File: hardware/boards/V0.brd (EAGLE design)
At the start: 134 parts, among them IC2 TPS6300, J1 SJ-43515TS-SMT, J2 HIROSE_DM3BT-DSF-PEJSHIROSE_D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, J3 MOLEX_105450-0101MOLEX_105450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, Q2 ON_SEMI_MMBT5551LT1GON_SEMI_M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, U1 VS1053-L, U2 MICROCHIP_MCP73831T-2ATI-OTMI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, X3 FH12-45S-0.5SH

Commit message: schematic: done!?
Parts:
- R31: value 1k -> 2k
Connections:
- removed net BLUE_LED_CATH: D1.1
- removed net IO18: R8.1, U$1.35
- removed net N$42: U1.30
- removed net N$43: U1.29
- removed net N$44: U1.28
- removed net N$45: U1.23
- removed net N$46: U1.13
- removed net N$47: U1.8
- removed net VDD_SDIO: U$1.26
- new net DREQ: U$1.15, U1.8
- new net SPI_MISO: U$1.38, U1.30, X3.29
- new net VIB_MOTOR: R8.1, U$1.29
- new net VS_CMD_CS: U$1.16, U1.23
- new net VS_DATA_CS: U$1.34, U1.13
- net ATQ_CHANGE: now also U$1.14
- net BUTTON_ADC: now also U$1.10
- net BUTTON_DIN: now also U$1.8
- net CP_VDD: no longer C24.+, C25.+, R31.2
- net DISPLAY_CS: now also U$1.12
- net DISPLAY_RST: now also U$1.13
- net GND: now also J2.12, J2.13, J2.14, X3.3; no longer X3.31, X3.33
- net GREEN_LED_CATH: now also U$1.28
- net I2C_SCL: now also U$1.39
- net I2C_SDA: now also U$1.42
- net IO0: now also D1.1
- net IO12: now also U$1.18
- net IO13: now also U$1.20
- net IO14: now also R7.2, U$1.17; no longer R6.2
- net IO15: now also R6.2, U$1.21; no longer R7.2
- net IO2: now also U$1.22
- net IO4: now also U$1.24
- net SPI_CLK: now also U$1.35, U1.28
- net SPI_MOSI: now also U$1.36, U1.29
- net V3P3: now also C24.+, C25.+, R31.2, X3.31, X3.33
- net VBAT_ADC_IN: now also U$1.7

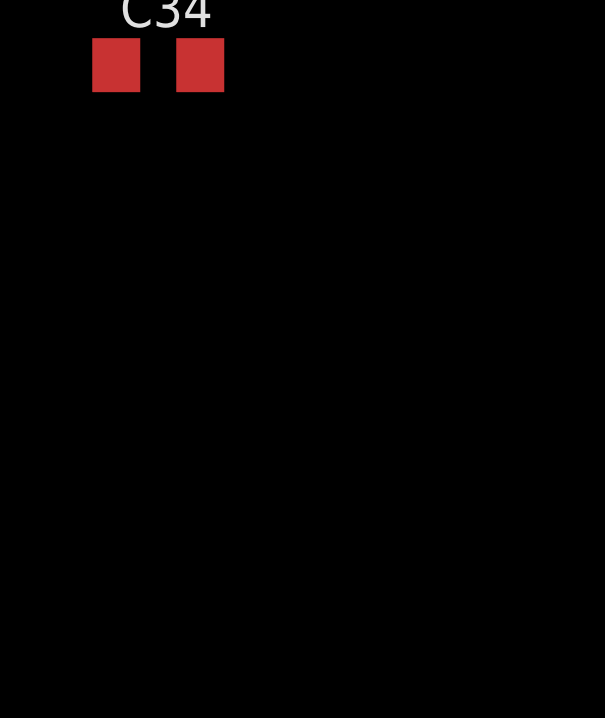
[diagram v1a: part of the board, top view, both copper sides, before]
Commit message: minor fixes: this is an adjustable 1.8V regulator..
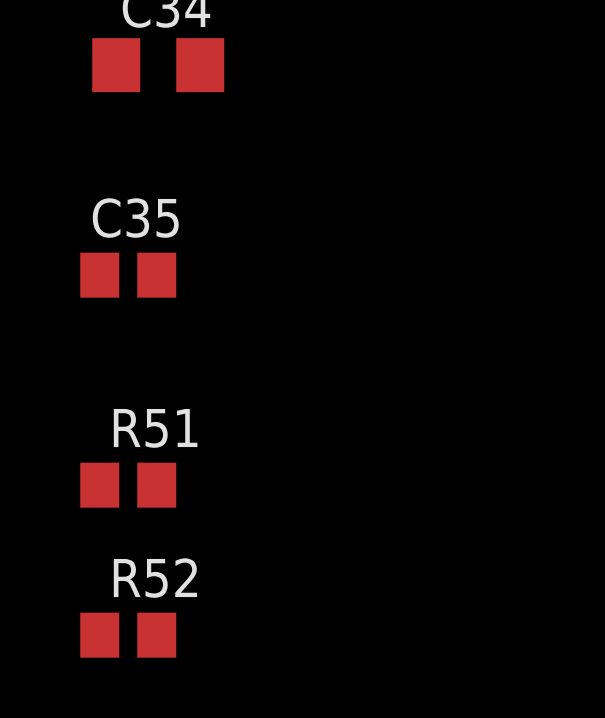
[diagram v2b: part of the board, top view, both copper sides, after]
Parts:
- added C35: 33pF, rcl:C0805
- added R51: 180k, rcl:R0805
- added R52: 360k, rcl:R0805
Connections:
- new net N$42: C35.2, R51.2, R52.1, TPS6224.5
- net GND: now also R51.1
- net V1P8: now also C35.1, R52.2; no longer TPS6224.5
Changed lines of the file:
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@@
 <attribute name="VALUE" x="-42.27" y="-778.54" size="1.27" layer="27"/>
+</element>
+<element name="C35" library="rcl" library_urn="urn:adsk.eagle:library:334" package="C0805" package3d_urn="urn:adsk.eagle:package:23617/2" value="33pF" x="-42" y="-783" smashed="yes">
+<attribute name="NAME" x="-43.27" y="-781.73" size="1.27" layer="25"/>
+<attribute name="SPICEPREFIX" value="C" x="-42" y="-783" size="1.778" layer="27" display="off"/>
+<attribute name="VALUE" x="-43.27" y="-785.54" size="1.27" layer="27"/>
+</element>
+<element name="R51" library="rcl" library_urn="urn:adsk.eagle:library:334" package="R0805" package3d_urn="urn:adsk.eagle:package:23553/2" value="180k" x="-42" y="-790" smashed="yes">
+<attribute name="NAME" x="-42.635" y="-788.73" size="1.27" layer="25"/>
+<attribute name="SPICEPREFIX" value="R" x="-42" y="-790" size="1.778" layer="27" display="off"/>
+<attribute name="VALUE" x="-42.635" y="-792.54" size="1.27" layer="27"/>
+</element>
+<element name="R52" library="rcl" library_urn="urn:adsk.eagle:library:334" package="R0805" package3d_urn="urn:adsk.eagle:package:23553/2" value="360k" x="-42" y="-795" smashed="yes">
+<attribute name="NAME" x="-42.635" y="-793.73" size="1.27" layer="25"/>
+<attribute name="SPICEPREFIX" value="R" x="-42" y="-795" size="1.778" layer="27" display="off"/>
+<attribute name="VALUE" x="-42.635" y="-797.54" size="1.27" layer="27"/>
 </element>
 </elements>
@@
 <contactref element="X3" pad="28"/>
 <contactref element="X3" pad="3"/>
+<contactref element="R51" pad="1"/>
 <wire x1="-21.275" y1="-222.175" x2="-28.675" y2="-222.175" width="0" layer="19" extent="1-1"/>
 <wire x1="-17.275" y1="-226.375" x2="-21.275" y2="-222.175" width="0" layer="19" extent="1-1"/>
@@
 <wire x1="-39.6" y1="-764" x2="-39.6" y2="-759" width="0" layer="19" extent="1-1"/>
 <wire x1="-39.6" y1="-776" x2="-39.6" y2="-764" width="0" layer="19" extent="1-1"/>
+<wire x1="-42.95" y1="-790" x2="-39.6" y2="-776" width="0" layer="19" extent="1-1"/>
 </signal>
 <signal name="N$22">
@@
 </signal>
 <signal name="V1P8">
-<contactref element="TPS6224" pad="5"/>
 <contactref element="U$5" pad="P$2"/>
 <contactref element="C18" pad="1"/>
@@
 <contactref element="TP2" pad="TP"/>
 <contactref element="C5" pad="1"/>
+<contactref element="C35" pad="1"/>
+<contactref element="R52" pad="2"/>
 <wire x1="-37.475" y1="-632" x2="-43" y2="-686" width="0" layer="19" extent="1-1"/>
+<wire x1="-42.95" y1="-783" x2="-43" y2="-686" width="0" layer="19" extent="1-1"/>
+<wire x1="-41.05" y1="-795" x2="-42.95" y2="-783" width="0" layer="19" extent="1-1"/>
 <wire x1="-20.7" y1="-336" x2="-37.475" y2="-632" width="0" layer="19" extent="1-1"/>
 <wire x1="-15.7" y1="-336" x2="-20.7" y2="-336" width="0" layer="19" extent="1-1"/>
@@
 <wire x1="-27.1" y1="-155.8" x2="-27.25" y2="-311.75" width="0" layer="19" extent="1-1"/>
 <wire x1="-30.4" y1="-143" x2="-27.1" y2="-155.8" width="0" layer="19" extent="1-1"/>
-<wire x1="-22.65" y1="-141.15" x2="-30.4" y2="-143" width="0" layer="19" extent="1-1"/>
 </signal>
 <signal name="N$3">
@@
 <wire x1="-14.725" y1="-7.75" x2="-23.95" y2="-81" width="0" layer="19" extent="1-1"/>
 </signal>
+<signal name="N$42">
+<contactref element="TPS6224" pad="5"/>
+<contactref element="R51" pad="2"/>
+<contactref element="C35" pad="2"/>
+<contactref element="R52" pad="1"/>
+<wire x1="-41.05" y1="-783" x2="-22.65" y2="-141.15" width="0" layer="19" extent="1-1"/>
+<wire x1="-41.05" y1="-790" x2="-41.05" y2="-783" width="0" layer="19" extent="1-1"/>
+<wire x1="-42.95" y1="-795" x2="-41.05" y2="-790" width="0" layer="19" extent="1-1"/>
+</signal>
 </signals>

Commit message: Power on/off changes + misc fixes
Corrected the power on/off circuit (connected the top of the switch to the right net) and bumped up the resistor value so that it'll take ~6 seconds of the power button being held down to power off.
The circuit should now match Figure 5 from [this](http://www.mosaic-industries.com/embedded-systems/microcontroller-projects/electronic-circuits/push-button-switch-turn-on/latching-toggle-power-switch).

This fixes #1.

Additionally, libraries used in the V0 files should match the rearranged folders.
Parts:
- R11: value 5M -> 10M
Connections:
- removed net CENTER_SW_PWR_BTM: CENTER_SW_PWR.4, CENTER_SW_PWR.4-2
- removed net N$12: C6.1, R10.1
- net CENTER_SW_PWR_TOP: now also C6.1, R10.1
- net GND: now also CENTER_SW_PWR.4, CENTER_SW_PWR.4-2
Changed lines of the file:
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@@
 <attribute name="VALUE" x="-22.775" y="-270.925" size="1.27" layer="27" rot="R90"/>
 </element>
-<element name="R11" library="rcl" library_urn="urn:adsk.eagle:library:334" package="R0805" package3d_urn="urn:adsk.eagle:package:23553/2" value="5M" x="-21" y="-275" smashed="yes">
+<element name="R11" library="rcl" library_urn="urn:adsk.eagle:library:334" package="R0805" package3d_urn="urn:adsk.eagle:package:23553/2" value="10M" x="-21" y="-275" smashed="yes">
 <attribute name="NAME" x="-22.397" y="-273.857" size="1.27" layer="25"/>
 <attribute name="SPICEPREFIX" value="R" x="-21" y="-275" size="1.778" layer="27" display="off"/>
@@
 <contactref element="X3" pad="3"/>
 <contactref element="R51" pad="1"/>
+<contactref element="CENTER_SW_PWR" pad="4"/>
+<contactref element="CENTER_SW_PWR" pad="4-2"/>
 <wire x1="-21.275" y1="-222.175" x2="-28.675" y2="-222.175" width="0" layer="19" extent="1-1"/>
 <wire x1="-17.275" y1="-226.375" x2="-21.275" y2="-222.175" width="0" layer="19" extent="1-1"/>
@@
 <wire x1="-35.05" y1="-548" x2="-35.05" y2="-541" width="0" layer="19" extent="1-1"/>
 <wire x1="-35.05" y1="-555" x2="-35.05" y2="-548" width="0" layer="19" extent="1-1"/>
-<wire x1="-42.525" y1="-632" x2="-35.05" y2="-555" width="0" layer="19" extent="1-1"/>
+<wire x1="-38.525" y1="-568.75" x2="-35.05" y2="-555" width="0" layer="19" extent="1-1"/>
+<wire x1="-38.875" y1="-568.75" x2="-38.525" y2="-568.75" width="0" layer="19" extent="1-1"/>
+<wire x1="-42.525" y1="-632" x2="-38.875" y2="-568.75" width="0" layer="19" extent="1-1"/>
 <wire x1="-42.525" y1="-638" x2="-42.525" y2="-632" width="0" layer="19" extent="1-1"/>
 <wire x1="-41.05" y1="-652" x2="-42.525" y2="-638" width="0" layer="19" extent="1-1"/>
@@
 <wire x1="-17.6" y1="-255" x2="-28.95" y2="-270.925" width="0" layer="19" extent="1-1"/>
 </signal>
-<signal name="N$12">
-<contactref element="R10" pad="1"/>
-<contactref element="C6" pad="1"/>
-<wire x1="-20.4" y1="-255" x2="-29.95" y2="-282" width="0" layer="19" extent="1-1"/>
-</signal>
 <signal name="N$14">
 <contactref element="C7" pad="2"/>
@@
 <contactref element="CENTER_SW_PWR" pad="2"/>
 <contactref element="R11" pad="1"/>
+<contactref element="R10" pad="1"/>
+<contactref element="C6" pad="1"/>
 <wire x1="-38.875" y1="-565.25" x2="-38.525" y2="-565.25" width="0" layer="19" extent="1-1"/>
-<wire x1="-21.95" y1="-275" x2="-38.525" y2="-565.25" width="0" layer="19" extent="1-1"/>
-</signal>
-<signal name="CENTER_SW_PWR_BTM">
-<contactref element="CENTER_SW_PWR" pad="4-2"/>
-<contactref element="CENTER_SW_PWR" pad="4"/>
-<wire x1="-38.875" y1="-568.75" x2="-38.525" y2="-568.75" width="0" layer="19" extent="1-1"/>
+<wire x1="-29.95" y1="-282" x2="-38.525" y2="-565.25" width="0" layer="19" extent="1-1"/>
+<wire x1="-21.95" y1="-275" x2="-29.95" y2="-282" width="0" layer="19" extent="1-1"/>
+<wire x1="-20.4" y1="-255" x2="-21.95" y2="-275" width="0" layer="19" extent="1-1"/>
 </signal>
 <signal name="N$18">

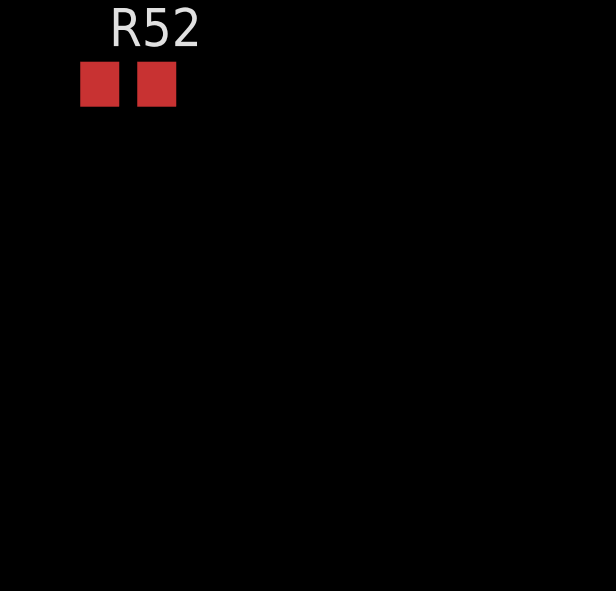
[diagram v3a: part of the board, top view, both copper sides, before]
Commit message: Add UVLO protection (using an APX809S-31SA)
Closes #4
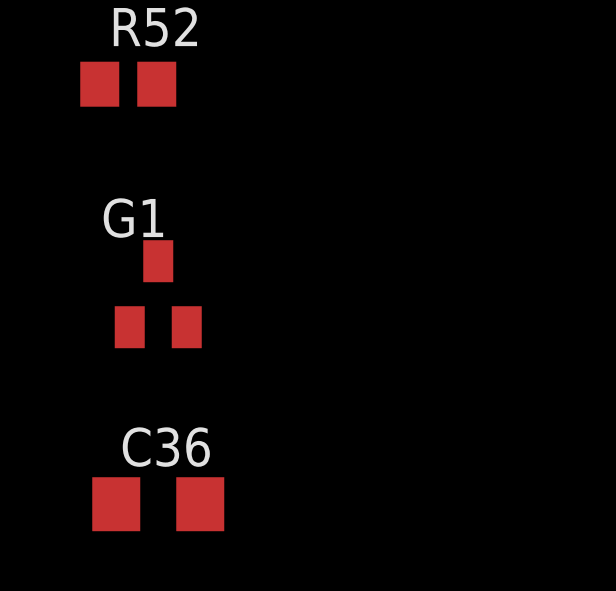
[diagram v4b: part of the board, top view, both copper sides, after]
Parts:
- added C36: 100nF, rcl:C1206
- added G1: APX809S-31SA, APX80xx:SOT23
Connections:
- new net N$12: U$2.3, U$2.5, U$2.7
- new net N$33: U$2.10, U$2.11, U$2.9
- new net N$43: G1.2, U$2.8
- net GND: now also C36.2, G1.1
- net SYS_ENABLE: now also U$2.12; no longer U$2.3, U$2.5
- net VBAT: now also C36.1, G1.3
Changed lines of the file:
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@@
 <attribute name="VALUE" x="-42.635" y="-797.54" size="1.27" layer="27"/>
+</element>
+<element name="G1" library="APX80xx" package="SOT23" package3d_urn="urn:adsk.eagle:package:28738/2" value="APX809S-31SA" x="-41" y="-802" smashed="yes">
+<attribute name="NAME" x="-42.905" y="-800.095" size="1.27" layer="25"/>
+<attribute name="VALUE" x="-42.905" y="-805.175" size="1.27" layer="27"/>
+</element>
+<element name="C36" library="rcl" library_urn="urn:adsk.eagle:library:334" package="C1206" package3d_urn="urn:adsk.eagle:package:23618/2" value="100nF" x="-41" y="-809" smashed="yes">
+<attribute name="NAME" x="-42.27" y="-807.73" size="1.27" layer="25"/>
+<attribute name="SPICEPREFIX" value="C" x="-41" y="-809" size="1.778" layer="27" display="off"/>
+<attribute name="VALUE" x="-42.27" y="-811.54" size="1.27" layer="27"/>
 </element>
 </elements>
@@
 <contactref element="CENTER_SW_PWR" pad="4"/>
 <contactref element="CENTER_SW_PWR" pad="4-2"/>
+<contactref element="G1" pad="1"/>
+<contactref element="C36" pad="2"/>
 <wire x1="-21.275" y1="-222.175" x2="-28.675" y2="-222.175" width="0" layer="19" extent="1-1"/>
 <wire x1="-17.275" y1="-226.375" x2="-21.275" y2="-222.175" width="0" layer="19" extent="1-1"/>
@@
 <wire x1="-39.6" y1="-776" x2="-39.6" y2="-764" width="0" layer="19" extent="1-1"/>
 <wire x1="-42.95" y1="-790" x2="-39.6" y2="-776" width="0" layer="19" extent="1-1"/>
+<wire x1="-41.95" y1="-803.1" x2="-42.95" y2="-790" width="0" layer="19" extent="1-1"/>
+<wire x1="-39.6" y1="-809" x2="-41.95" y2="-803.1" width="0" layer="19" extent="1-1"/>
 </signal>
 <signal name="N$22">
@@
 <contactref element="R10" pad="2"/>
 <contactref element="R9" pad="2"/>
+<contactref element="G1" pad="3"/>
+<contactref element="C36" pad="1"/>
 <wire x1="-18.05" y1="-156" x2="-27.5" y2="-162.95" width="0" layer="19" extent="1-1"/>
 <wire x1="-24.85" y1="-150" x2="-18.05" y2="-156" width="0" layer="19" extent="1-1"/>
@@
 <wire x1="-35.2" y1="-536.95" x2="-35.05" y2="-529" width="0" layer="19" extent="1-1"/>
 <wire x1="-36.95" y1="-541" x2="-35.2" y2="-536.95" width="0" layer="19" extent="1-1"/>
+<wire x1="-41" y1="-800.9" x2="-36.95" y2="-541" width="0" layer="19" extent="1-1"/>
+<wire x1="-42.4" y1="-809" x2="-41" y2="-800.9" width="0" layer="19" extent="1-1"/>
 </signal>
 <signal name="V3P3">
@@
 <signal name="SYS_ENABLE">
 <contactref element="IC2" pad="6"/>
-<contactref element="U$2" pad="3"/>
-<contactref element="U$2" pad="5"/>
-<wire x1="-26.35" y1="-270.925" x2="-18" y2="-128.525" width="0" layer="19" extent="1-1"/>
-<wire x1="-27.65" y1="-270.925" x2="-26.35" y2="-270.925" width="0" layer="19" extent="1-1"/>
+<contactref element="U$2" pad="12"/>
+<wire x1="-27.65" y1="-265.075" x2="-18" y2="-128.525" width="0" layer="19" extent="1-1"/>
 </signal>
 <signal name="CENTER_SW_PWR_TOP">
@@
 <wire x1="-42.95" y1="-795" x2="-41.05" y2="-790" width="0" layer="19" extent="1-1"/>
 </signal>
+<signal name="N$12">
+<contactref element="U$2" pad="3"/>
+<contactref element="U$2" pad="5"/>
+<contactref element="U$2" pad="7"/>
+<wire x1="-26.35" y1="-270.925" x2="-27.65" y2="-270.925" width="0" layer="19" extent="1-1"/>
+<wire x1="-25.05" y1="-270.925" x2="-26.35" y2="-270.925" width="0" layer="19" extent="1-1"/>
+</signal>
+<signal name="N$33">
+<contactref element="U$2" pad="9"/>
+<contactref element="U$2" pad="11"/>
+<contactref element="U$2" pad="10"/>
+<wire x1="-26.35" y1="-265.075" x2="-25.7" y2="-265.075" width="0" layer="19" extent="1-1"/>
+<wire x1="-27" y1="-265.075" x2="-26.35" y2="-265.075" width="0" layer="19" extent="1-1"/>
+</signal>
+<signal name="N$43">
+<contactref element="G1" pad="2"/>
+<contactref element="U$2" pad="8"/>
+<wire x1="-25.05" y1="-265.075" x2="-40.05" y2="-803.1" width="0" layer="19" extent="1-1"/>
+</signal>
 </signals>
